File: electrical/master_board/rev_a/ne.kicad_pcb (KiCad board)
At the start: 2 copper layers, 42.2 x 39 mm, 1 part, among them CN60 HCSR04;F1x4H

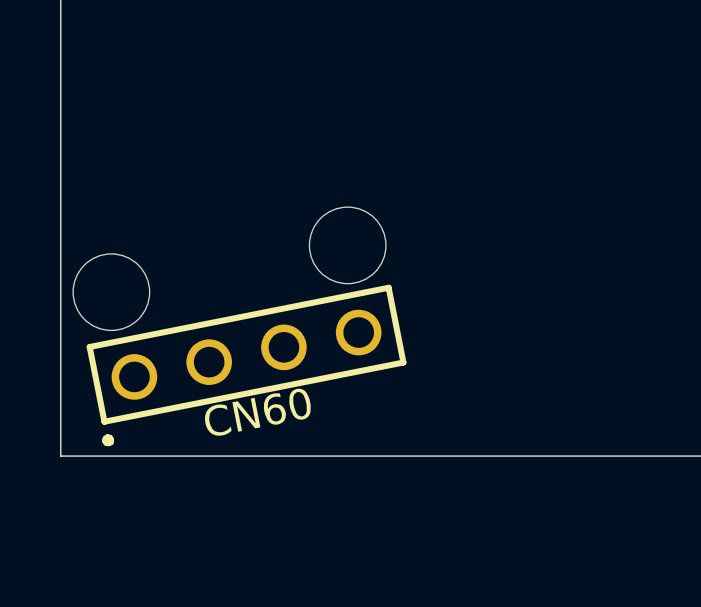
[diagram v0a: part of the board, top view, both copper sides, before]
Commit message: The PCBChunk'ification of Sonars is complete.
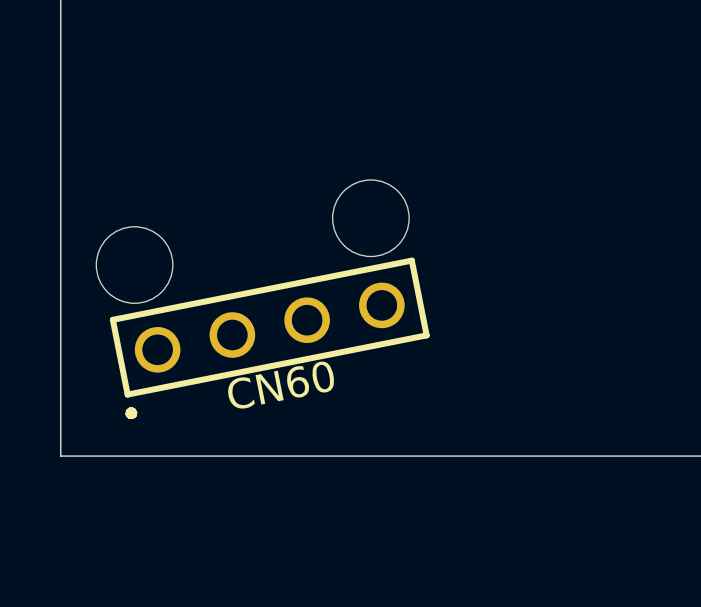
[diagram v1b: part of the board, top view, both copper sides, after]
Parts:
- moved CN60 1.19 mm to (137.0, 56.7)
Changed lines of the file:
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@@
     (uvia_dia 0.3)
     (uvia_drill 0.1)
+    (add_net "Net-(CN60-Pad1)")
+    (add_net "Net-(CN60-Pad2)")
+    (add_net "Net-(CN60-Pad3)")
+    (add_net "Net-(CN60-Pad4)")
   )
   (module HR2:HCSR04_F1x4H (layer F.Cu)
-    (at 136.1937 57.6226 191.2)
+    (at 136.9666 56.7177 191.2)
     (fp_text reference CN60 (at 0 -2 11.2) (layer F.SilkS)
       (effects (font (size 1 1) (thickness 0.2)))
@@
       (effects (font (size 1 1) (thickness 0.2)))
     )
+    (fp_line (start -5.08 -1.27) (end 5.08 -1.27) (layer F.SilkS) (width 0.2))
+    (fp_line (start -5.08 1.27) (end -5.08 -1.27) (layer F.SilkS) (width 0.2))
+    (fp_line (start 5.08 1.27) (end -5.08 1.27) (layer F.SilkS) (width 0.2))
+    (fp_line (start 5.08 -1.27) (end 5.08 1.27) (layer F.SilkS) (width 0.2))
+    (fp_line (start 5.15 -1.83) (end 5.18 -1.91) (layer F.SilkS) (width 0.2))
+    (fp_line (start 5.08 -1.8) (end 5.15 -1.83) (layer F.SilkS) (width 0.2))
+    (fp_line (start 5.01 -1.83) (end 5.08 -1.8) (layer F.SilkS) (width 0.2))
+    (fp_line (start 4.98 -1.91) (end 5.01 -1.83) (layer F.SilkS) (width 0.2))
+    (fp_line (start 5.01 -1.98) (end 4.98 -1.91) (layer F.SilkS) (width 0.2))
+    (fp_line (start 5.08 -2) (end 5.01 -1.98) (layer F.SilkS) (width 0.2))
+    (fp_line (start 5.15 -1.98) (end 5.08 -2) (layer F.SilkS) (width 0.2))
     (fp_line (start 5.18 -1.91) (end 5.15 -1.98) (layer F.SilkS) (width 0.2))
-    (fp_line (start 5.15 -1.98) (end 5.08 -2) (layer F.SilkS) (width 0.2))
-    (fp_line (start 5.08 -2) (end 5.01 -1.98) (layer F.SilkS) (width 0.2))
-    (fp_line (start 5.01 -1.98) (end 4.98 -1.91) (layer F.SilkS) (width 0.2))
-    (fp_line (start 4.98 -1.91) (end 5.01 -1.83) (layer F.SilkS) (width 0.2))
-    (fp_line (start 5.01 -1.83) (end 5.08 -1.8) (layer F.SilkS) (width 0.2))
-    (fp_line (start 5.08 -1.8) (end 5.15 -1.83) (layer F.SilkS) (width 0.2))
-    (fp_line (start 5.15 -1.83) (end 5.18 -1.91) (layer F.SilkS) (width 0.2))
-    (fp_line (start 5.08 -1.27) (end 5.08 1.27) (layer F.SilkS) (width 0.2))
-    (fp_line (start 5.08 1.27) (end -5.08 1.27) (layer F.SilkS) (width 0.2))
-    (fp_line (start -5.08 1.27) (end -5.08 -1.27) (layer F.SilkS) (width 0.2))
-    (fp_line (start -5.08 -1.27) (end 5.08 -1.27) (layer F.SilkS) (width 0.2))
     (pad "HCSR04 West Tie Down Hole (High)" np_thru_hole circle (at -4.015 2.921 191.2) (size 2.55 2.55) (drill 2.55) (layers *.Cu *.Mask))
     (pad "HCSR04 East Tie Down Hole (Hight)" np_thru_hole circle (at 4.015 2.921 191.2) (size 2.55 2.55) (drill 2.55) (layers *.Cu *.Mask))

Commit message: Finally have everything fitting together.
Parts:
- moved CN60 3.97 mm to (138.1, 60.5)
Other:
- outline, holes or cut-outs redrawn
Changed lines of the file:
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@@
   )
   (module HR2:HCSR04_F1x4H (layer F.Cu)
-    (at 136.9666 56.7177 191.2)
+    (at 138.1284 60.5169 191.2)
     (fp_text reference CN60 (at 0 -2 11.2) (layer F.SilkS)
       (effects (font (size 1 1) (thickness 0.2)))
@@
   (gr_line (start 130.02 26.19) (end 130.01 26.33) (layer Edge.Cuts) (width 0.05))
   (gr_line (start 130.01 26.33) (end 130 26.46) (layer Edge.Cuts) (width 0.05))
-  (gr_line (start 130 26.46) (end 130 61) (layer Edge.Cuts) (width 0.05))
-  (gr_line (start 130 61) (end 161 61) (layer Edge.Cuts) (width 0.05))
-  (gr_line (start 161 61) (end 161.13 61.01) (layer Edge.Cuts) (width 0.05))
-  (gr_line (start 161.13 61.01) (end 161.26 61.02) (layer Edge.Cuts) (width 0.05))
-  (gr_line (start 161.26 61.02) (end 161.39 61.05) (layer Edge.Cuts) (width 0.05))
-  (gr_line (start 161.39 61.05) (end 161.51 61.09) (layer Edge.Cuts) (width 0.05))
-  (gr_line (start 161.51 61.09) (end 161.63 61.14) (layer Edge.Cuts) (width 0.05))
-  (gr_line (start 161.63 61.14) (end 161.75 61.2) (layer Edge.Cuts) (width 0.05))
-  (gr_line (start 161.75 61.2) (end 161.86 61.27) (layer Edge.Cuts) (width 0.05))
-  (gr_line (start 161.86 61.27) (end 161.96 61.35) (layer Edge.Cuts) (width 0.05))
-  (gr_line (start 161.96 61.35) (end 162.06 61.44) (layer Edge.Cuts) (width 0.05))
-  (gr_line (start 162.06 61.44) (end 162.15 61.54) (layer Edge.Cuts) (width 0.05))
-  (gr_line (start 162.15 61.54) (end 162.23 61.64) (layer Edge.Cuts) (width 0.05))
-  (gr_line (start 162.23 61.64) (end 162.3 61.75) (layer Edge.Cuts) (width 0.05))
-  (gr_line (start 162.3 61.75) (end 162.36 61.87) (layer Edge.Cuts) (width 0.05))
-  (gr_line (start 162.36 61.87) (end 162.41 61.99) (layer Edge.Cuts) (width 0.05))
-  (gr_line (start 162.41 61.99) (end 162.45 62.11) (layer Edge.Cuts) (width 0.05))
-  (gr_line (start 162.45 62.11) (end 162.48 62.24) (layer Edge.Cuts) (width 0.05))
-  (gr_line (start 162.48 62.24) (end 162.49 62.37) (layer Edge.Cuts) (width 0.05))
-  (gr_line (start 162.49 62.37) (end 162.5 62.5) (layer Edge.Cuts) (width 0.05))
-  (gr_line (start 162.5 62.5) (end 162.5 64) (layer Edge.Cuts) (width 0.05))
+  (gr_line (start 130 26.46) (end 130 61.5) (layer Edge.Cuts) (width 0.05))
+  (gr_line (start 130 61.5) (end 161 61.5) (layer Edge.Cuts) (width 0.05))
+  (gr_line (start 161 61.5) (end 161.13 61.51) (layer Edge.Cuts) (width 0.05))
+  (gr_line (start 161.13 61.51) (end 161.26 61.52) (layer Edge.Cuts) (width 0.05))
+  (gr_line (start 161.26 61.52) (end 161.39 61.55) (layer Edge.Cuts) (width 0.05))
+  (gr_line (start 161.39 61.55) (end 161.51 61.59) (layer Edge.Cuts) (width 0.05))
+  (gr_line (start 161.51 61.59) (end 161.63 61.64) (layer Edge.Cuts) (width 0.05))
+  (gr_line (start 161.63 61.64) (end 161.75 61.7) (layer Edge.Cuts) (width 0.05))
+  (gr_line (start 161.75 61.7) (end 161.86 61.77) (layer Edge.Cuts) (width 0.05))
+  (gr_line (start 161.86 61.77) (end 161.96 61.85) (layer Edge.Cuts) (width 0.05))
+  (gr_line (start 161.96 61.85) (end 162.06 61.94) (layer Edge.Cuts) (width 0.05))
+  (gr_line (start 162.06 61.94) (end 162.15 62.04) (layer Edge.Cuts) (width 0.05))
+  (gr_line (start 162.15 62.04) (end 162.23 62.14) (layer Edge.Cuts) (width 0.05))
+  (gr_line (start 162.23 62.14) (end 162.3 62.25) (layer Edge.Cuts) (width 0.05))
+  (gr_line (start 162.3 62.25) (end 162.36 62.37) (layer Edge.Cuts) (width 0.05))
+  (gr_line (start 162.36 62.37) (end 162.41 62.49) (layer Edge.Cuts) (width 0.05))
+  (gr_line (start 162.41 62.49) (end 162.45 62.61) (layer Edge.Cuts) (width 0.05))
+  (gr_line (start 162.45 62.61) (end 162.48 62.74) (layer Edge.Cuts) (width 0.05))
+  (gr_line (start 162.48 62.74) (end 162.49 62.87) (layer Edge.Cuts) (width 0.05))
+  (gr_line (start 162.49 62.87) (end 162.5 63) (layer Edge.Cuts) (width 0.05))
+  (gr_line (start 162.5 63) (end 162.5 64) (layer Edge.Cuts) (width 0.05))
 )

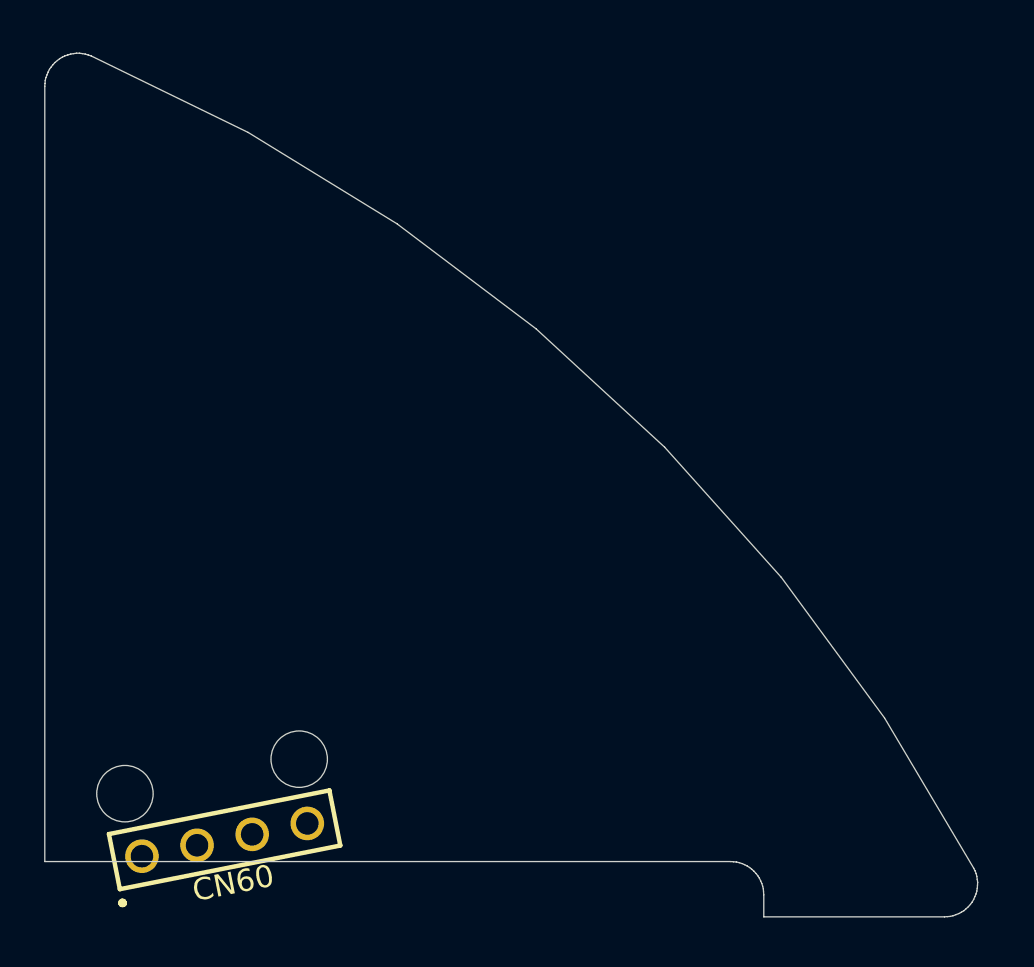
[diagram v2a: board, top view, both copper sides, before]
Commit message: Added spacer mounting holes to schematics and associated PCB's.
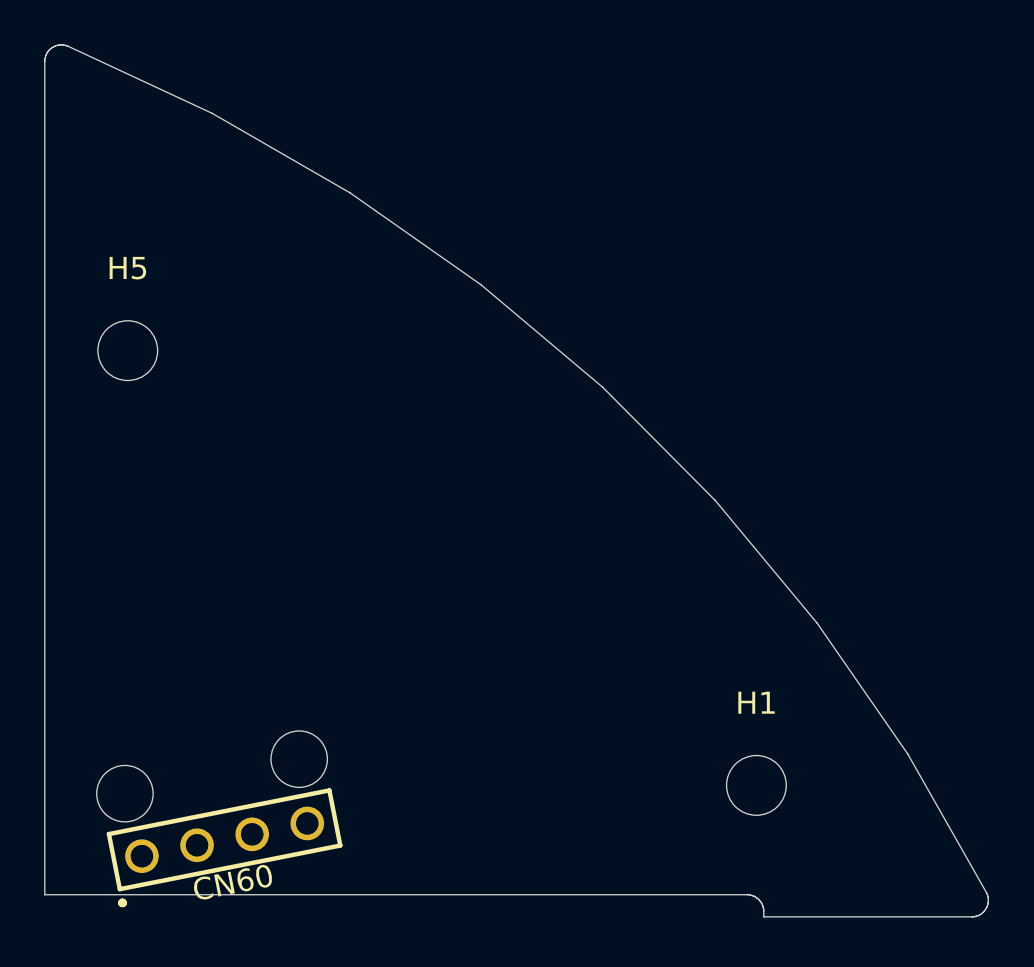
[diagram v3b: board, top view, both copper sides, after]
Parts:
- added H1: HOLE;M2.5, MountingHole:MountingHole_2.7mm_M2.5, F.Cu at (162.2, 58.1)
- added H5: HOLE;M2.5, MountingHole:MountingHole_2.7mm_M2.5, F.Cu at (133.8, 38.4)
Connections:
- CN60 pad 1: (no net) -> Net-(CN60-Pad1)
- CN60 pad 2: (no net) -> Net-(CN60-Pad2)
- CN60 pad 3: (no net) -> Net-(CN60-Pad3)
- CN60 pad 4: (no net) -> Net-(CN60-Pad4)
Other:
- board size 42.2 x 39 mm -> 42.7 x 39.4 mm

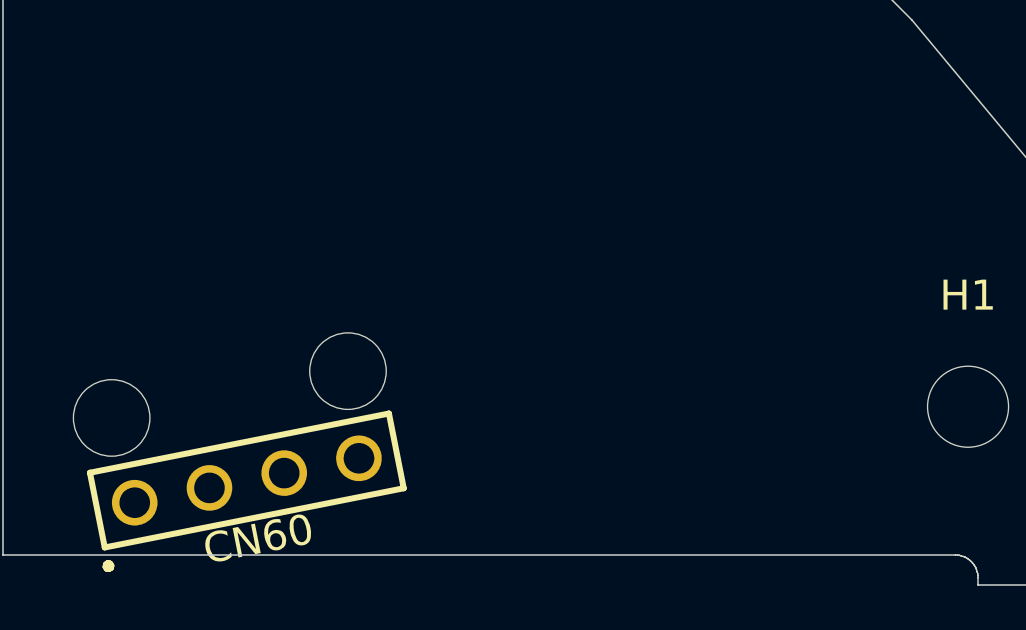
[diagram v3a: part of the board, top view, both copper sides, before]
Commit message: Placed all of the Groves on the PCB's.
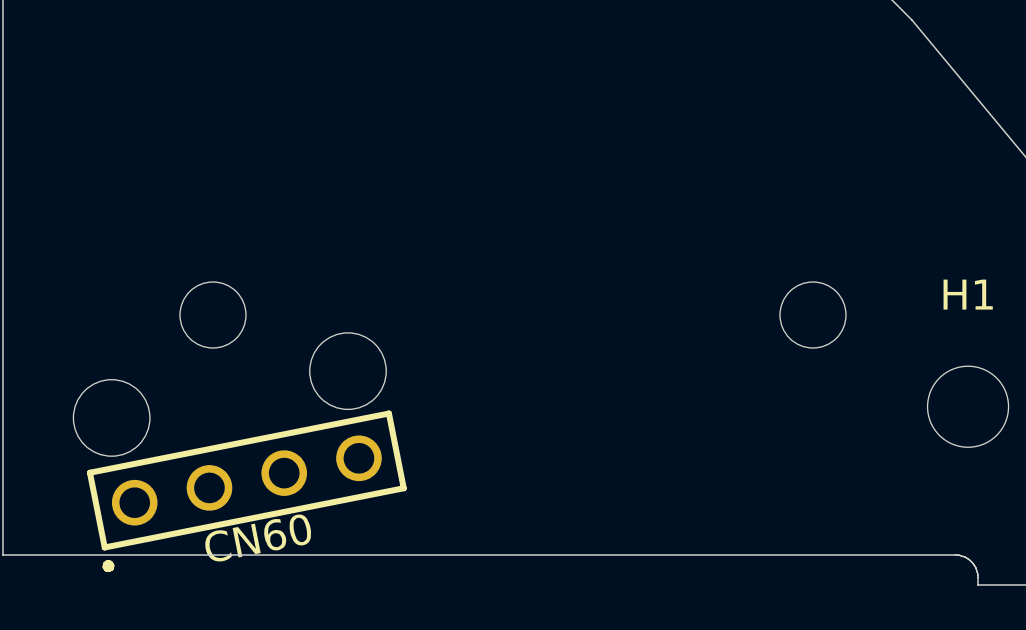
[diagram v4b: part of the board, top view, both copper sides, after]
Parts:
- added GV2: GROVE;20x20, HR2:GROVE20x20, B.Cu at (147.0, 55.0)
